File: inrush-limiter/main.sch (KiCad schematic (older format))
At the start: 27 parts, among them K1 RELAY_2RT, P1 CONN_01X04, P2 CONN_01X02, Q1 PN2222A, Q2 PN2222A, U1 LM393

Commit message: update
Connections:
- wire segments 93 -> 66
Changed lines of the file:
@@
 $EndComp
 Wire Wire Line
-	1550 2250 1800 2250
-Wire Wire Line
-	1800 2250 1900 2250
+	1550 2250 1900 2250
 Wire Wire Line
 	1800 2250 1800 2700
@@
 Connection ~ 1800 2250
 Wire Wire Line
-	2200 2250 2350 2250
-Wire Wire Line
-	2350 2250 3000 2250
+	2200 2250 3000 2250
 Wire Wire Line
 	2200 2700 2350 2700
@@
 	3000 2250 3000 2450
 Wire Wire Line
-	2950 2450 3000 2450
-Wire Wire Line
-	3000 2450 3050 2450
+	2950 2450 3050 2450
 Connection ~ 3000 2450
 Wire Wire Line
-	2650 2450 2650 2650
+	2650 2450 2650 2850
 Wire Wire Line
-	2650 2650 2650 2850
+	3350 2450 3350 2850
 Wire Wire Line
-	3350 2450 3350 2650
-Wire Wire Line
-	3350 2650 3350 2850
-Wire Wire Line
-	2950 2850 3000 2850
-Wire Wire Line
-	3000 2850 3050 2850
+	2950 2850 3050 2850
 Wire Wire Line
 	3000 3050 3000 2850
@@
 Connection ~ 2650 2650
 Wire Wire Line
-	3350 2650 3750 2650
-Wire Wire Line
-	3750 2650 4400 2650
-Wire Wire Line
-	4400 2650 4950 2650
+	3350 2650 4950 2650
 Connection ~ 3350 2650
 Wire Wire Line
@@
 Connection ~ 3750 2650
 Wire Wire Line
-	4400 3050 4400 3100
+	4400 3050 4400 3150
 Wire Wire Line
-	4400 3100 4400 3150
-Wire Wire Line
-	2500 3550 3750 3550
-Wire Wire Line
-	3750 3550 4400 3550
-Wire Wire Line
-	4400 3550 4950 3550
+	2500 3550 4950 3550
 Wire Wire Line
 	4400 3100 4650 3100
@@
 Connection ~ 4400 2650
 Wire Wire Line
-	4950 3300 4950 3550
-Wire Wire Line
-	4950 3550 4950 3750
+	4950 3300 4950 3750
 Wire Wire Line
 	3750 3550 3750 3200
@@
 	3300 4750 3400 4750
 Wire Wire Line
-	1150 4100 1750 4100
+	1150 4100 4750 4100
 Wire Wire Line
-	1750 4100 2500 4100
-Wire Wire Line
-	2500 4100 4750 4100
-Wire Wire Line
-	1750 4500 1750 4850
-Wire Wire Line
-	1750 4850 1750 4950
+	1750 4500 1750 4950
 Wire Wire Line
 	2300 4850 1750 4850
@@
 	1750 5350 1750 5250
 Wire Wire Line
-	1150 5350 1450 5350
-Wire Wire Line
-	1450 5350 1750 5350
-Wire Wire Line
-	1750 5350 2500 5350
-Wire Wire Line
-	2500 5350 3700 5350
+	1150 5350 3700 5350
 Connection ~ 2500 5350
 Wire Wire Line
-	1150 4000 1150 4100
-Wire Wire Line
-	1150 4100 1150 4200
+	1150 4000 1150 4200
 Connection ~ 1750 4100
 Wire Wire Line
-	1150 4500 1150 4650
+	1150 4500 1150 4950
 Wire Wire Line
-	1150 4650 1150 4950
-Wire Wire Line
-	1150 5250 1150 5350
-Wire Wire Line
-	1150 5350 1150 5500
+	1150 5250 1150 5500
 Connection ~ 1750 5350
 Connection ~ 1150 5350
 Wire Wire Line
-	1150 4650 1450 4650
-Wire Wire Line
-	1450 4650 2300 4650
+	1150 4650 2300 4650
 Connection ~ 1150 4650
 Connection ~ 2500 4100
@@
 	4750 4400 4600 4400
 Wire Wire Line
-	5550 4300 6200 4300
-Wire Wire Line
-	6200 4300 6450 4300
+	5550 4300 6450 4300
 Wire Wire Line
 	5550 4500 5700 4500
 Wire Wire Line
-	4950 2450 4950 2650
-Wire Wire Line
-	4950 2650 4950 2900
+	4950 2450 4950 2900
 Connection ~ 4950 2650
 Wire Wire Line
@@
 	2500 1200 2000 1200
 Wire Wire Line
-	1350 1350 2000 1350
-Wire Wire Line
-	2000 1350 2100 1350
+	1350 1350 2100 1350
 Wire Wire Line
 	2400 1350 2500 1350
@@
 	2000 1050 2100 1050
 Wire Wire Line
-	2000 1200 2000 1350
-Wire Wire Line
-	2000 1350 2000 1450
+	2000 1200 2000 1450
 Connection ~ 2000 1350
 Wire Wire Line
 	2400 1050 2500 1050
 Wire Wire Line
-	1900 900  2000 900
-Wire Wire Line
-	2000 900  2500 900
+	1900 900  2500 900
 Wire Wire Line
 	2000 900  2000 1050

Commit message: add leds
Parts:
- removed P2: CONN_01X02, Pin_Headers:Pin_Header_Straight_1x02, symbol CONN_01X02
- added D6, D?: LED, symbol LED
- added R13, R?: 140, symbol R
- Q1, Q2: footprint TO_SOT_Packages_THT:TO-92_Inline_Narrow_Oval -> TO_SOT_Packages_THT:TO-92_Inline_Wide
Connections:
- wire segments 66 -> 72
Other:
- moved on the sheet: K1, Q1, R10
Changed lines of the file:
@@
 F 0 "Q2" H 5050 3175 50  0000 L CNN
 F 1 "PN2222A" H 5050 3100 50  0000 L CNN
-F 2 "TO_SOT_Packages_THT:TO-92_Inline_Narrow_Oval" H 5050 3025 50  0001 L CIN
+F 2 "TO_SOT_Packages_THT:TO-92_Inline_Wide" H 5050 3025 50  0001 L CIN
 F 3 "" H 4850 3100 50  0000 L CNN
 	1    4850 3100
@@
 $EndComp
 $Comp
-L GND #PWR01
-U 1 1 57C1A76B
-P 4950 3750
-F 0 "#PWR01" H 4950 3500 50  0001 C CNN
-F 1 "GND" H 4950 3600 50  0000 C CNN
-F 2 "" H 4950 3750 50  0000 C CNN
-F 3 "" H 4950 3750 50  0000 C CNN
-	1    4950 3750
-	1    0    0    -1
-$EndComp
-$Comp
-L +5V #PWR02
+L +5V #PWR6
 U 1 1 57C1A7D8
 P 4950 2450
-F 0 "#PWR02" H 4950 2300 50  0001 C CNN
+F 0 "#PWR6" H 4950 2300 50  0001 C CNN
 F 1 "+5V" H 4950 2590 50  0000 C CNN
 F 2 "" H 4950 2450 50  0000 C CNN
@@
 $EndComp
 $Comp
-L +5V #PWR03
+L +5V #PWR1
 U 1 1 57C1B997
 P 1150 3550
-F 0 "#PWR03" H 1150 3400 50  0001 C CNN
+F 0 "#PWR1" H 1150 3400 50  0001 C CNN
 F 1 "+5V" H 1150 3690 50  0000 C CNN
 F 2 "" H 1150 3550 50  0000 C CNN
@@
 $EndComp
 $Comp
-L GND #PWR04
+L GND #PWR2
 U 1 1 57C1BA06
 P 1150 5500
-F 0 "#PWR04" H 1150 5250 50  0001 C CNN
+F 0 "#PWR2" H 1150 5250 50  0001 C CNN
 F 1 "GND" H 1150 5350 50  0000 C CNN
 F 2 "" H 1150 5500 50  0000 C CNN
@@
 L PN2222A Q1
 U 1 1 57C1BB6B
-P 3600 4750
-F 0 "Q1" H 3800 4825 50  0000 L CNN
-F 1 "PN2222A" H 3800 4750 50  0000 L CNN
-F 2 "TO_SOT_Packages_THT:TO-92_Inline_Narrow_Oval" H 3800 4675 50  0001 L CIN
-F 3 "" H 3600 4750 50  0000 L CNN
-	1    3600 4750
-	1    0    0    -1
+P 3700 4950
+F 0 "Q1" H 3900 5025 50  0000 L CNN
+F 1 "PN2222A" H 3900 4950 50  0000 L CNN
+F 2 "TO_SOT_Packages_THT:TO-92_Inline_Wide" H 3900 4875 50  0001 L CIN
+F 3 "" H 3700 4950 50  0000 L CNN
+	1    3700 4950
+	0    1    1    0
 $EndComp
 $Comp
@@
 Text GLabel 2500 900  2    60   Input ~ 0
 AC-live-f
-Text GLabel 4600 4400 0    60   Input ~ 0
+Text GLabel 5150 4400 0    60   Input ~ 0
 AC-live-f
 $Comp
 L R R10
 U 1 1 57C2C65A
-P 5850 4500
-F 0 "R10" V 5930 4500 50  0000 C CNN
-F 1 "100, 5W" V 5850 4500 50  0000 C CNN
-F 2 "Resistors_ThroughHole:Resistor_Horizontal_RM25mm" V 5780 4500 50  0001 C CNN
-F 3 "" H 5850 4500 50  0000 C CNN
-	1    5850 4500
+P 6400 4500
+F 0 "R10" V 6480 4500 50  0000 C CNN
+F 1 "100, 5W" V 6400 4500 50  0000 C CNN
+F 2 "Resistors_ThroughHole:Resistor_Horizontal_RM25mm" V 6330 4500 50  0001 C CNN
+F 3 "" H 6400 4500 50  0000 C CNN
+	1    6400 4500
 	0    -1   -1   0
 $EndComp
-Text GLabel 6450 4300 2    60   Input ~ 0
+Text GLabel 7000 4300 2    60   Input ~ 0
 AC-live-out
 $Comp
-L +5V #PWR05
+L +5V #PWR3
 U 1 1 57C33EC3
-P 4250 1200
-F 0 "#PWR05" H 4250 1050 50  0001 C CNN
-F 1 "+5V" H 4250 1340 50  0000 C CNN
-F 2 "" H 4250 1200 50  0000 C CNN
-F 3 "" H 4250 1200 50  0000 C CNN
-	1    4250 1200
-	1    0    0    -1
-$EndComp
-$Comp
-L GND #PWR06
+P 3850 850
+F 0 "#PWR3" H 3850 700 50  0001 C CNN
+F 1 "+5V" H 3850 990 50  0000 C CNN
+F 2 "" H 3850 850 50  0000 C CNN
+F 3 "" H 3850 850 50  0000 C CNN
+	1    3850 850
+	1    0    0    -1
+$EndComp
+$Comp
+L GND #PWR4
 U 1 1 57C33F05
-P 4250 1500
-F 0 "#PWR06" H 4250 1250 50  0001 C CNN
-F 1 "GND" H 4250 1350 50  0000 C CNN
-F 2 "" H 4250 1500 50  0000 C CNN
-F 3 "" H 4250 1500 50  0000 C CNN
-	1    4250 1500
+P 3850 1850
+F 0 "#PWR4" H 3850 1600 50  0001 C CNN
+F 1 "GND" H 3850 1700 50  0000 C CNN
+F 2 "" H 3850 1850 50  0000 C CNN
+F 3 "" H 3850 1850 50  0000 C CNN
+	1    3850 1850
 	1    0    0    -1
 $EndComp
@@
 L RELAY_2RT K1
 U 1 1 57C3B514
-P 5150 4450
-F 0 "K1" H 5100 4850 50  0000 C CNN
-F 1 "RELAY_2RT" H 5300 3950 50  0000 C CNN
-F 2 "Relays_ThroughHole:Relay_DPDT_Schrack-RT2_RM5mm" H 5150 4450 50  0001 C CNN
-F 3 "" H 5150 4450 50  0000 C CNN
-	1    5150 4450
+P 5700 4450
+F 0 "K1" H 5650 4850 50  0000 C CNN
+F 1 "RELAY_2RT" H 5850 3950 50  0000 C CNN
+F 2 "Relays_ThroughHole:Relay_DPDT_Schrack-RT2_RM5mm" H 5700 4450 50  0001 C CNN
+F 3 "" H 5700 4450 50  0000 C CNN
+	1    5700 4450
 	1    0    0    1
 $EndComp
@@
 Text GLabel 2500 1200 2    60   Input ~ 0
 AC-neut
-$Comp
-L CONN_01X02 P2
-U 1 1 57C3DE82
-P 4050 1350
-F 0 "P2" H 4050 1650 50  0000 C CNN
-F 1 "CONN_01X02" V 4150 1350 50  0000 C CNN
-F 2 "Pin_Headers:Pin_Header_Straight_1x02" H 4050 1350 50  0001 C CNN
-F 3 "" H 4050 1350 50  0000 C CNN
-	1    4050 1350
-	-1   0    0    1
-$EndComp
 $Comp
 L CONN_01X04 P1
@@
 	2900 4750 3000 4750
 Wire Wire Line
-	3300 4750 3400 4750
-Wire Wire Line
-	1150 4100 4750 4100
+	3300 4750 3700 4750
+Wire Wire Line
+	1700 4100 5300 4100
 Wire Wire Line
 	1750 4500 1750 4950
@@
 	1750 5350 1750 5250
 Wire Wire Line
-	1150 5350 3700 5350
+	1150 5350 3500 5350
 Connection ~ 2500 5350
 Wire Wire Line
@@
 Connection ~ 1150 4100
 Wire Wire Line
-	4750 4200 3700 4200
-Wire Wire Line
-	3700 4200 3700 4550
-Wire Wire Line
-	3700 5350 3700 4950
-Wire Wire Line
 	1550 3050 1900 3050
 Wire Wire Line
-	4750 4400 4600 4400
-Wire Wire Line
-	5550 4300 6450 4300
-Wire Wire Line
-	5550 4500 5700 4500
+	5300 4400 5150 4400
+Wire Wire Line
+	6100 4300 7000 4300
+Wire Wire Line
+	6100 4500 6250 4500
 Wire Wire Line
 	4950 2450 4950 2900
 Connection ~ 4950 2650
 Wire Wire Line
-	4250 1500 4250 1400
-Wire Wire Line
-	4250 1300 4250 1200
-Wire Wire Line
-	6200 4300 6200 4500
-Wire Wire Line
-	6200 4500 6000 4500
-Connection ~ 6200 4300
+	3850 1850 3850 1750
+Wire Wire Line
+	3850 950  3850 850
+Wire Wire Line
+	6750 4300 6750 4500
+Wire Wire Line
+	6750 4500 6550 4500
+Connection ~ 6750 4300
 Wire Wire Line
 	1150 3550 1150 3700
@@
 Connection ~ 4400 3550
 Wire Wire Line
-	2500 5050 2500 5350
-Wire Wire Line
-	2500 4450 2500 4100
+	2500 5350 2500 5050
+Wire Wire Line
+	2500 4100 2500 4450
 Wire Wire Line
 	1350 1550 2500 1550
@@
 	1350 900  1350 1250
 $Comp
-L Earth #PWR07
+L Earth #PWR5
 U 1 1 57C44B9E
-P 5500 1100
-F 0 "#PWR07" H 5500 850 50  0001 C CNN
-F 1 "Earth" H 5500 950 50  0001 C CNN
-F 2 "" H 5500 1100 50  0000 C CNN
-F 3 "" H 5500 1100 50  0000 C CNN
-	1    5500 1100
-	1    0    0    -1
-$EndComp
-Wire Wire Line
-	5650 1050 5500 1050
-Wire Wire Line
-	5500 1050 5500 1100
+P 4350 1100
+F 0 "#PWR5" H 4350 850 50  0001 C CNN
+F 1 "Earth" H 4350 950 50  0001 C CNN
+F 2 "" H 4350 1100 50  0000 C CNN
+F 3 "" H 4350 1100 50  0000 C CNN
+	1    4350 1100
+	1    0    0    -1
+$EndComp
+Wire Wire Line
+	4500 1050 4350 1050
+Wire Wire Line
+	4350 1050 4350 1100
+$Comp
+L R R13
+U 1 1 57C48F41
+P 3850 1100
+F 0 "R13" V 3930 1100 50  0000 C CNN
+F 1 "140" V 3850 1100 50  0000 C CNN
+F 2 "" V 3780 1100 50  0000 C CNN
+F 3 "" H 3850 1100 50  0000 C CNN
+	1    3850 1100
+	1    0    0    -1
+$EndComp
+$Comp
+L LED D6
+U 1 1 57C49062
+P 3850 1550
+F 0 "D6" H 3850 1650 50  0000 C CNN
+F 1 "LED" H 3850 1450 50  0000 C CNN
+F 2 "" H 3850 1550 50  0000 C CNN
+F 3 "" H 3850 1550 50  0000 C CNN
+	1    3850 1550
+	0    -1   -1   0
+$EndComp
+Wire Wire Line
+	3850 1350 3850 1250
+Wire Wire Line
+	3900 5350 5250 5350
+Wire Wire Line
+	3900 5050 3900 5350
+Wire Wire Line
+	3500 5350 3500 5050
+$Comp
+L R R?
+U 1 1 57C521F5
+P 4150 4450
+F 0 "R?" V 4230 4450 50  0000 C CNN
+F 1 "140" V 4150 4450 50  0000 C CNN
+F 2 "" V 4080 4450 50  0000 C CNN
+F 3 "" H 4150 4450 50  0000 C CNN
+	1    4150 4450
+	1    0    0    -1
+$EndComp
+$Comp
+L LED D?
+U 1 1 57C53617
+P 4150 4950
+F 0 "D?" H 4150 5050 50  0000 C CNN
+F 1 "LED" H 4150 4850 50  0000 C CNN
+F 2 "" H 4150 4950 50  0000 C CNN
+F 3 "" H 4150 4950 50  0000 C CNN
+	1    4150 4950
+	0    -1   -1   0
+$EndComp
+Wire Wire Line
+	4150 4300 4150 4100
+Connection ~ 4150 4100
+Wire Wire Line
+	4150 4600 4150 4750
+Wire Wire Line
+	4150 5150 4150 5350
+Connection ~ 4150 5350
+Wire Wire Line
+	5300 4200 5250 4200
+Wire Wire Line
+	5250 4200 5250 5350
 $EndSCHEMATC

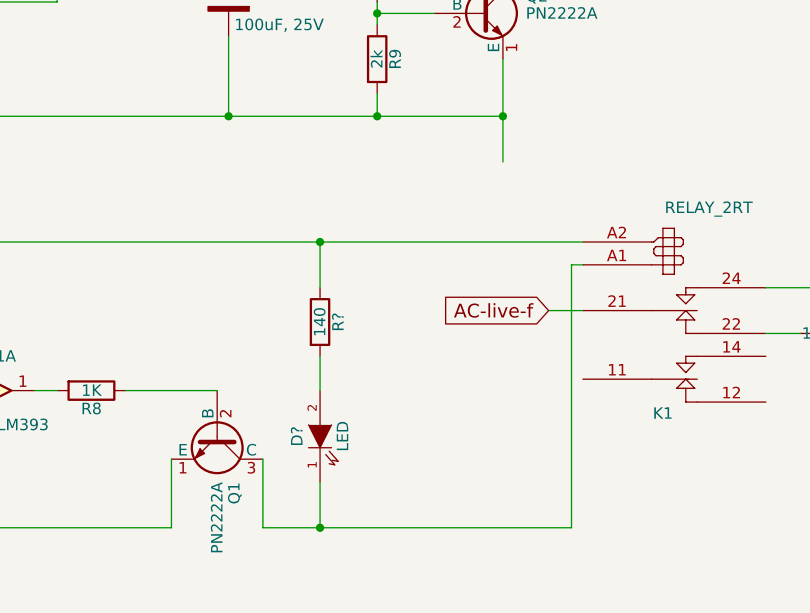
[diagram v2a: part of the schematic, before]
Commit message: add leds
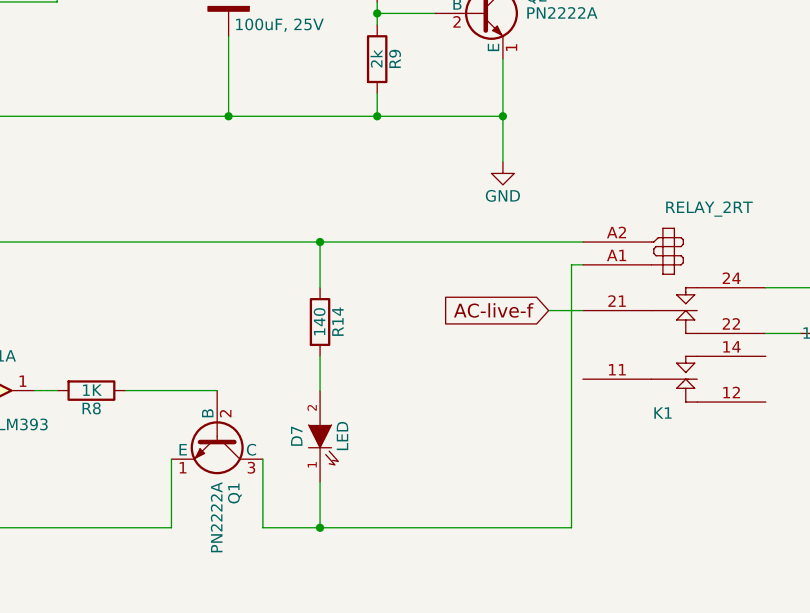
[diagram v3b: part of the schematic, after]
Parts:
- D6: footprint (none) -> LEDs:LED-5MM
- D7: renamed from D?; footprint (none) -> LEDs:LED-5MM
- R13: footprint (none) -> Resistors_ThroughHole:Resistor_Horizontal_RM7mm
- R14: renamed from R?; footprint (none) -> Resistors_ThroughHole:Resistor_Horizontal_RM7mm
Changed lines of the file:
@@
 $EndComp
 $Comp
-L +5V #PWR6
+L +5V #PWR01
 U 1 1 57C1A7D8
 P 4950 2450
-F 0 "#PWR6" H 4950 2300 50  0001 C CNN
+F 0 "#PWR01" H 4950 2300 50  0001 C CNN
 F 1 "+5V" H 4950 2590 50  0000 C CNN
 F 2 "" H 4950 2450 50  0000 C CNN
@@
 $EndComp
 $Comp
-L +5V #PWR1
+L +5V #PWR02
 U 1 1 57C1B997
 P 1150 3550
-F 0 "#PWR1" H 1150 3400 50  0001 C CNN
+F 0 "#PWR02" H 1150 3400 50  0001 C CNN
 F 1 "+5V" H 1150 3690 50  0000 C CNN
 F 2 "" H 1150 3550 50  0000 C CNN
@@
 $EndComp
 $Comp
-L GND #PWR2
+L GND #PWR03
 U 1 1 57C1BA06
 P 1150 5500
-F 0 "#PWR2" H 1150 5250 50  0001 C CNN
+F 0 "#PWR03" H 1150 5250 50  0001 C CNN
 F 1 "GND" H 1150 5350 50  0000 C CNN
 F 2 "" H 1150 5500 50  0000 C CNN
@@
 AC-live-out
 $Comp
-L +5V #PWR3
+L +5V #PWR04
 U 1 1 57C33EC3
 P 3850 850
-F 0 "#PWR3" H 3850 700 50  0001 C CNN
+F 0 "#PWR04" H 3850 700 50  0001 C CNN
 F 1 "+5V" H 3850 990 50  0000 C CNN
 F 2 "" H 3850 850 50  0000 C CNN
@@
 $EndComp
 $Comp
-L GND #PWR4
+L GND #PWR05
 U 1 1 57C33F05
 P 3850 1850
-F 0 "#PWR4" H 3850 1600 50  0001 C CNN
+F 0 "#PWR05" H 3850 1600 50  0001 C CNN
 F 1 "GND" H 3850 1700 50  0000 C CNN
 F 2 "" H 3850 1850 50  0000 C CNN
@@
 	1350 900  1350 1250
 $Comp
-L Earth #PWR5
+L Earth #PWR06
 U 1 1 57C44B9E
 P 4350 1100
-F 0 "#PWR5" H 4350 850 50  0001 C CNN
+F 0 "#PWR06" H 4350 850 50  0001 C CNN
 F 1 "Earth" H 4350 950 50  0001 C CNN
 F 2 "" H 4350 1100 50  0000 C CNN
@@
 F 0 "R13" V 3930 1100 50  0000 C CNN
 F 1 "140" V 3850 1100 50  0000 C CNN
-F 2 "" V 3780 1100 50  0000 C CNN
+F 2 "Resistors_ThroughHole:Resistor_Horizontal_RM7mm" V 3780 1100 50  0001 C CNN
 F 3 "" H 3850 1100 50  0000 C CNN
 	1    3850 1100
@@
 F 0 "D6" H 3850 1650 50  0000 C CNN
 F 1 "LED" H 3850 1450 50  0000 C CNN
-F 2 "" H 3850 1550 50  0000 C CNN
+F 2 "LEDs:LED-5MM" H 3850 1550 50  0001 C CNN
 F 3 "" H 3850 1550 50  0000 C CNN
 	1    3850 1550
@@
 	3500 5350 3500 5050
 $Comp
-L R R?
+L R R14
 U 1 1 57C521F5
 P 4150 4450
-F 0 "R?" V 4230 4450 50  0000 C CNN
+F 0 "R14" V 4230 4450 50  0000 C CNN
 F 1 "140" V 4150 4450 50  0000 C CNN
-F 2 "" V 4080 4450 50  0000 C CNN
+F 2 "Resistors_ThroughHole:Resistor_Horizontal_RM7mm" V 4080 4450 50  0001 C CNN
 F 3 "" H 4150 4450 50  0000 C CNN
 	1    4150 4450
@@
 $EndComp
 $Comp
-L LED D?
+L LED D7
 U 1 1 57C53617
 P 4150 4950
-F 0 "D?" H 4150 5050 50  0000 C CNN
+F 0 "D7" H 4150 5050 50  0000 C CNN
 F 1 "LED" H 4150 4850 50  0000 C CNN
-F 2 "" H 4150 4950 50  0000 C CNN
+F 2 "LEDs:LED-5MM" H 4150 4950 50  0001 C CNN
 F 3 "" H 4150 4950 50  0000 C CNN
 	1    4150 4950
@@
 Wire Wire Line
 	5250 4200 5250 5350
+$Comp
+L GND #PWR?
+U 1 1 57C55E64
+P 4950 3750
+F 0 "#PWR?" H 4950 3500 50  0001 C CNN
+F 1 "GND" H 4950 3600 50  0000 C CNN
+F 2 "" H 4950 3750 50  0000 C CNN
+F 3 "" H 4950 3750 50  0000 C CNN
+	1    4950 3750
+	1    0    0    -1
+$EndComp
 $EndSCHEMATC

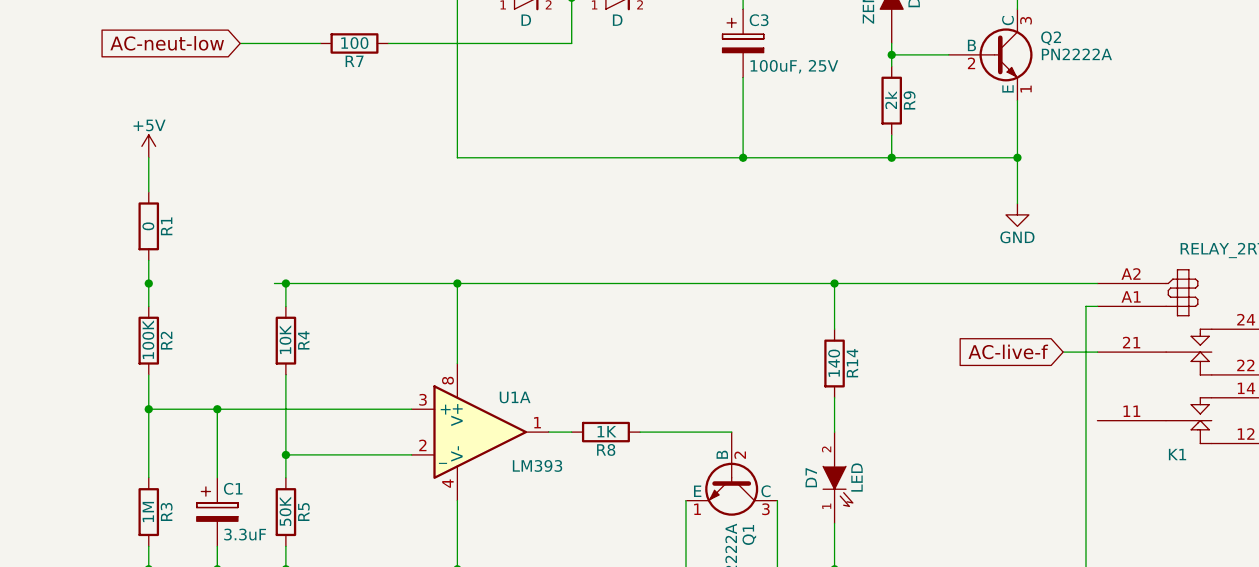
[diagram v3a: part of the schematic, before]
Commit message: fix missing 5v supply
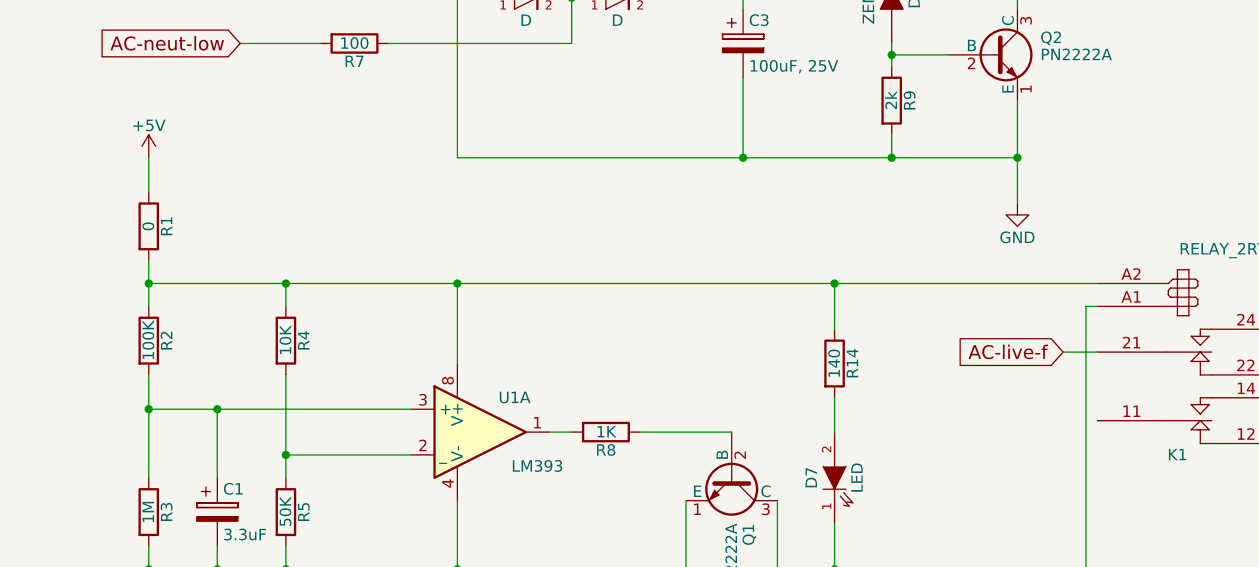
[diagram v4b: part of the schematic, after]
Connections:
- net at K1.A2 (9), R14.1, R4.1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: now also R1.2, R2.1
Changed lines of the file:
@@
 	3300 4750 3700 4750
 Wire Wire Line
-	1700 4100 5300 4100
+	1150 4100 5300 4100
 Wire Wire Line
 	1750 4500 1750 4950
@@
 	5250 4200 5250 5350
 $Comp
-L GND #PWR?
+L GND #PWR07
 U 1 1 57C55E64
 P 4950 3750
-F 0 "#PWR?" H 4950 3500 50  0001 C CNN
+F 0 "#PWR07" H 4950 3500 50  0001 C CNN
 F 1 "GND" H 4950 3600 50  0000 C CNN
 F 2 "" H 4950 3750 50  0000 C CNN
